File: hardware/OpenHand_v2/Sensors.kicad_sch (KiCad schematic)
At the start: 56 parts, among them U5 LM324, U6 LM324

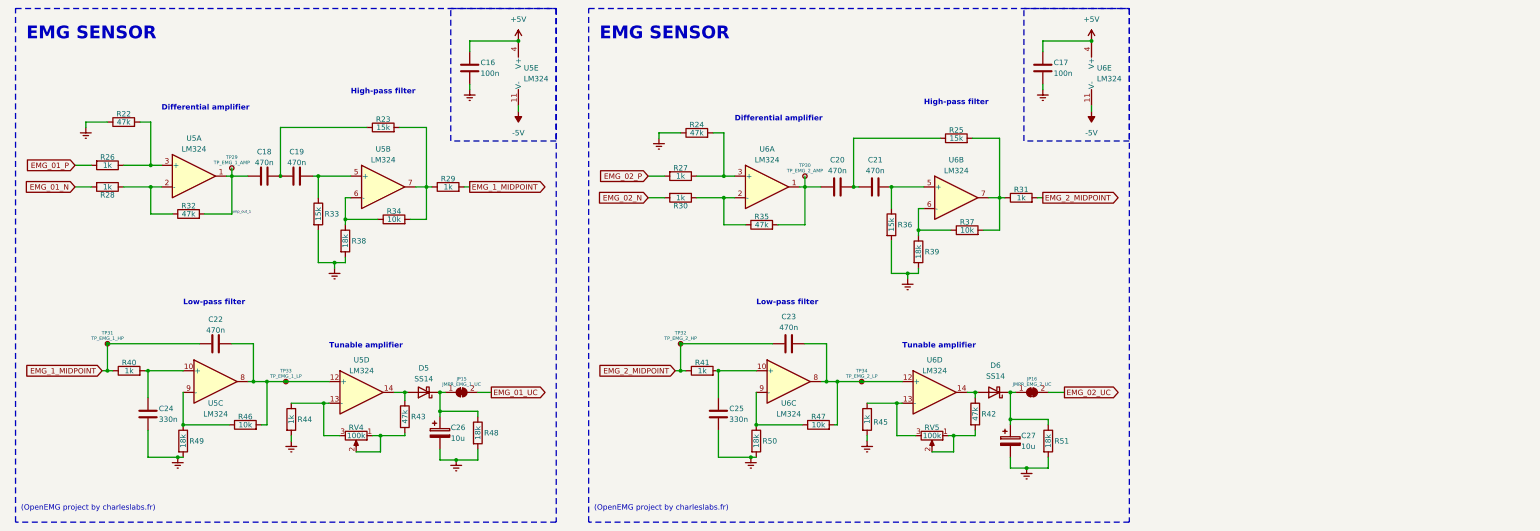
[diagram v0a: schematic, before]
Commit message: Update V2 schematic and start PCB layout
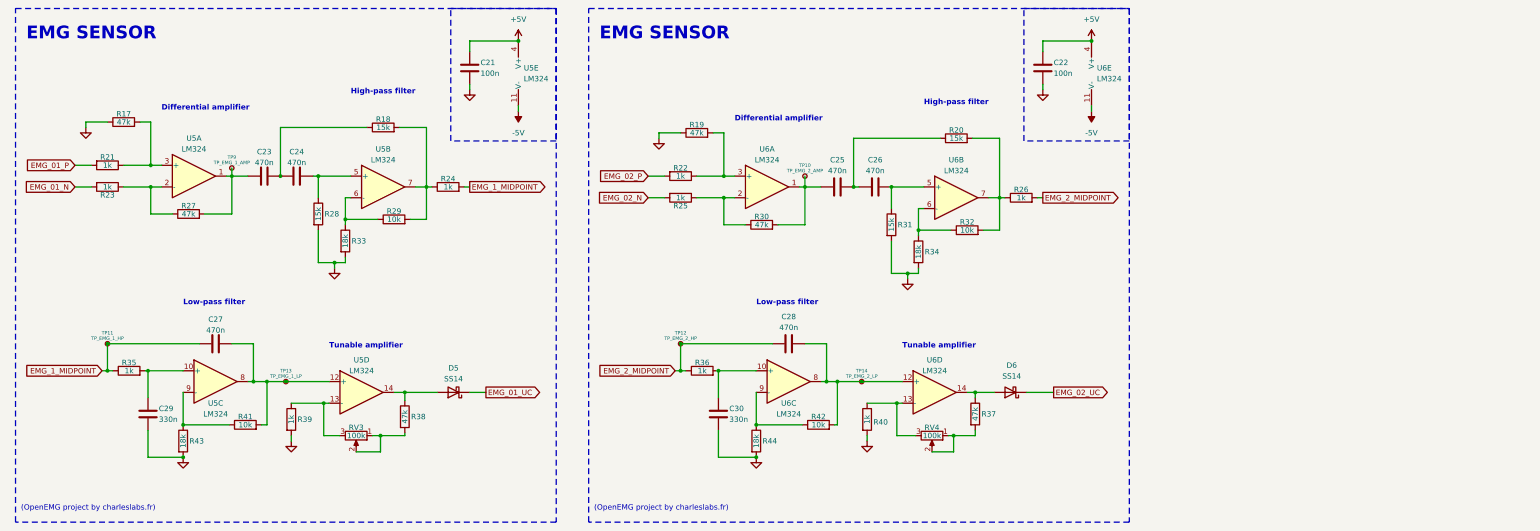
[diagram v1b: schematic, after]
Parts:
- removed C26, C27: 10u, Capacitor_SMD:C_0805_2012Metric, symbol Device:C_Polarized
- removed JP15: JMPR_EMG_1_UC, Jumper:SolderJumper-2_P1.3mm_Bridged_RoundedPad1.0x1.5mm, symbol Jumper:SolderJumper_2_Bridged
- removed JP16: JMPR_EMG_2_UC, Jumper:SolderJumper-2_P1.3mm_Bridged_RoundedPad1.0x1.5mm, symbol Jumper:SolderJumper_2_Bridged
- removed R48, R51: 18k, Resistor_SMD:R_0805_2012Metric, symbol Device:R
- renumbered C16 to C21, C17 to C22, C18 to C23, C19 to C24, C20 to C25, C21 to C26, C22 to C27, C23 to C28, C24 to C29, C25 to C30, R22 to R17, R23 to R18, R24 to R19, R25 to R20, R26 to R21, R27 to R22, R28 to R23, R29 to R24, R30 to R25, R31 to R26, R32 to R27, R33 to R28, R34 to R29, R35 to R30, R36 to R31, R37 to R32, R38 to R33, R39 to R34, R40 to R35, R41 to R36, R42 to R37, R43 to R38, R44 to R39, R45 to R40, R46 to R41, R47 to R42, R49 to R43, R50 to R44, RV4 to RV3, RV5 to RV4, TP30 to TP10, TP31 to TP11, TP32 to TP12, TP33 to TP13, TP34 to TP14, TP29 to TP9
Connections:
- net EMG_01_UC: now also D5.1 (K)
- net EMG_02_UC: now also D6.1 (K)
- net Earth renamed GND
- net amp_out_1: no longer names the net of C23.1, R27.2, TP9.1, U5.1
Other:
- moved on the sheet: D5, D6

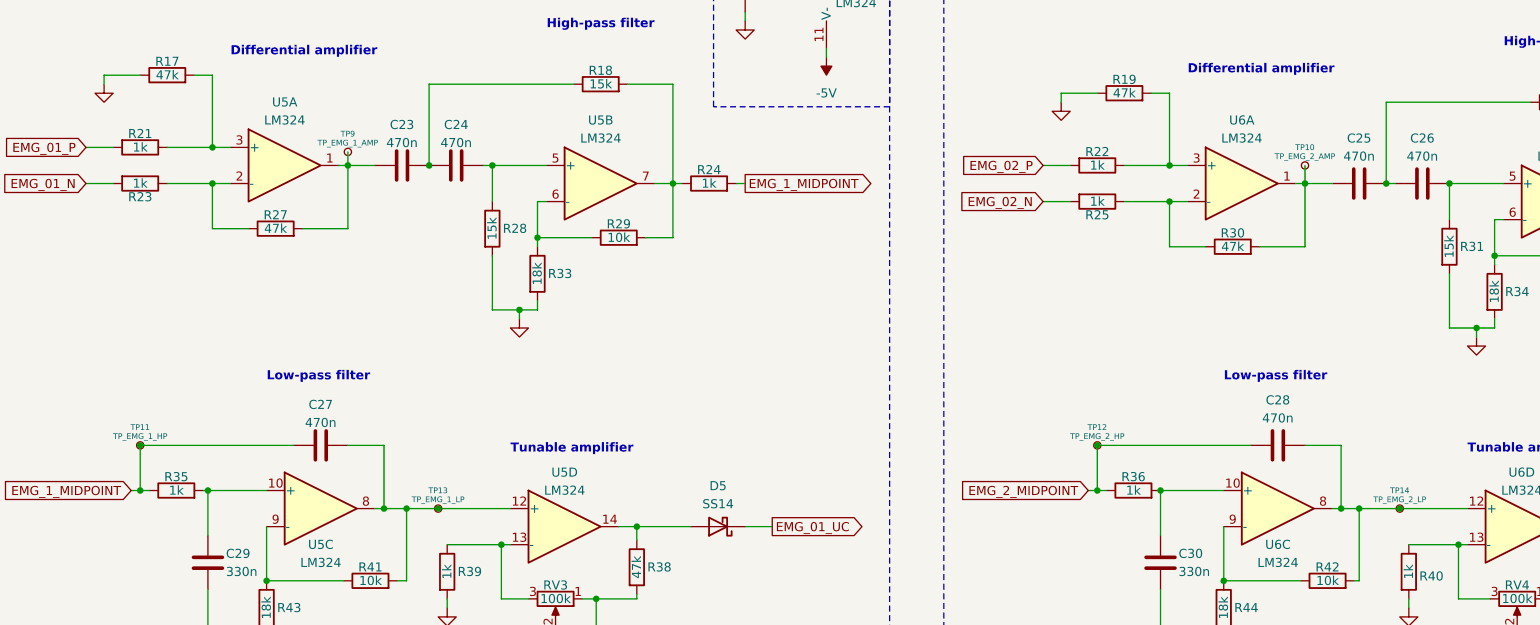
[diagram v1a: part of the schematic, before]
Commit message: Add V2 PCB and update CubeIDE config for V2
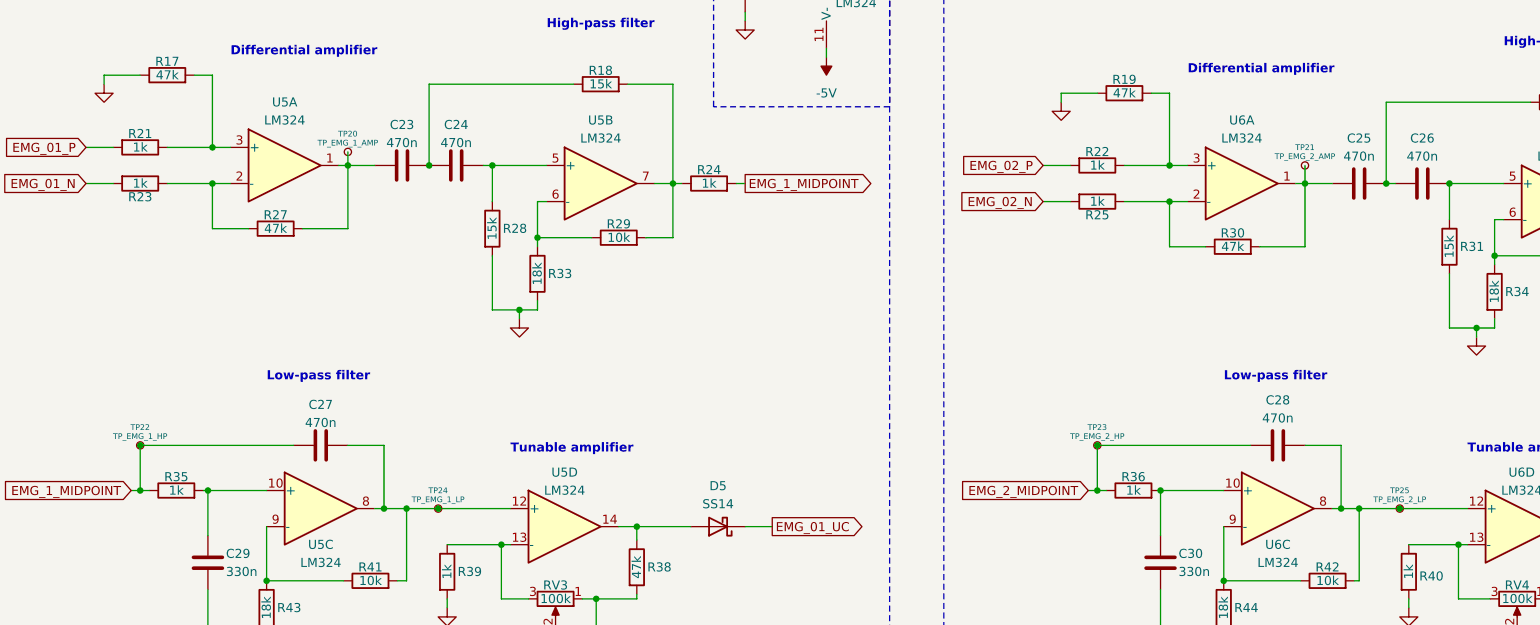
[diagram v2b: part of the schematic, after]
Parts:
- renumbered TP9 to TP20, TP10 to TP21, TP11 to TP22, TP12 to TP23, TP13 to TP24, TP14 to TP25
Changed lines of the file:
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@@
 		(dnp no)
 		(fields_autoplaced yes)
-		(property "Reference" "#PWR051"
+		(property "Reference" "#PWR053"
 			(at 270.51 29.21 0)
 			(effects
@@
 			(project "OpenHand_v2"
 				(path "/f1fbd835-8408-4592-854c-2fbec9d052ec/286dde41-8068-419e-b7de-6276970410d8"
-					(reference "#PWR051")
+					(reference "#PWR053")
 					(unit 1)
 				)
@@
 		(dnp no)
 		(fields_autoplaced yes)
-		(property "Reference" "#PWR053"
+		(property "Reference" "#PWR055"
 			(at 259.08 43.18 0)
 			(effects
@@
 			(project "OpenHand_v2"
 				(path "/f1fbd835-8408-4592-854c-2fbec9d052ec/286dde41-8068-419e-b7de-6276970410d8"
-					(reference "#PWR053")
+					(reference "#PWR055")
 					(unit 1)
 				)
@@
 		(dnp no)
 		(fields_autoplaced yes)
-		(property "Reference" "#PWR063"
+		(property "Reference" "#PWR065"
 			(at 191.77 129.54 0)
 			(effects
@@
 			(project "OpenHand_v2"
 				(path "/f1fbd835-8408-4592-854c-2fbec9d052ec/286dde41-8068-419e-b7de-6276970410d8"
-					(reference "#PWR063")
+					(reference "#PWR065")
 					(unit 1)
 				)
@@
 		(on_board yes)
 		(dnp no)
-		(property "Reference" "TP11"
+		(property "Reference" "TP22"
 			(at 39.37 93.98 0)
 			(effects
@@
 			(project "OpenHand_v2"
 				(path "/f1fbd835-8408-4592-854c-2fbec9d052ec/286dde41-8068-419e-b7de-6276970410d8"
-					(reference "TP11")
+					(reference "TP22")
 					(unit 1)
 				)
@@
 		(dnp no)
 		(fields_autoplaced yes)
-		(property "Reference" "#PWR057"
+		(property "Reference" "#PWR059"
 			(at 168.91 54.61 0)
 			(effects
@@
 			(project "OpenHand_v2"
 				(path "/f1fbd835-8408-4592-854c-2fbec9d052ec/286dde41-8068-419e-b7de-6276970410d8"
-					(reference "#PWR057")
+					(reference "#PWR059")
 					(unit 1)
 				)
@@
 		(on_board yes)
 		(dnp no)
-		(property "Reference" "TP13"
+		(property "Reference" "TP24"
 			(at 81.28 102.87 0)
 			(effects
@@
 			(project "OpenHand_v2"
 				(path "/f1fbd835-8408-4592-854c-2fbec9d052ec/286dde41-8068-419e-b7de-6276970410d8"
-					(reference "TP13")
+					(reference "TP24")
 					(unit 1)
 				)
@@
 		(dnp no)
 		(fields_autoplaced yes)
-		(property "Reference" "#PWR061"
+		(property "Reference" "#PWR063"
 			(at 217.805 125.73 0)
 			(effects
@@
 			(project "OpenHand_v2"
 				(path "/f1fbd835-8408-4592-854c-2fbec9d052ec/286dde41-8068-419e-b7de-6276970410d8"
-					(reference "#PWR061")
+					(reference "#PWR063")
 					(unit 1)
 				)
@@
 		(dnp no)
 		(fields_autoplaced yes)
-		(property "Reference" "#PWR052"
+		(property "Reference" "#PWR054"
 			(at 124.46 43.18 0)
 			(effects
@@
 			(project "OpenHand_v2"
 				(path "/f1fbd835-8408-4592-854c-2fbec9d052ec/286dde41-8068-419e-b7de-6276970410d8"
-					(reference "#PWR052")
+					(reference "#PWR054")
 					(unit 1)
 				)
@@
 		(on_board yes)
 		(dnp no)
-		(property "Reference" "TP14"
+		(property "Reference" "TP25"
 			(at 216.535 102.87 0)
 			(effects
@@
 			(project "OpenHand_v2"
 				(path "/f1fbd835-8408-4592-854c-2fbec9d052ec/286dde41-8068-419e-b7de-6276970410d8"
-					(reference "TP14")
+					(reference "TP25")
 					(unit 1)
 				)
@@
 		(dnp no)
 		(fields_autoplaced yes)
-		(property "Reference" "#PWR055"
+		(property "Reference" "#PWR057"
 			(at 270.51 44.45 0)
 			(effects
@@
 			(project "OpenHand_v2"
 				(path "/f1fbd835-8408-4592-854c-2fbec9d052ec/286dde41-8068-419e-b7de-6276970410d8"
-					(reference "#PWR055")
+					(reference "#PWR057")
 					(unit 1)
 				)
@@
 		(dnp no)
 		(fields_autoplaced yes)
-		(property "Reference" "#PWR062"
+		(property "Reference" "#PWR064"
 			(at 57.15 129.54 0)
 			(effects
@@
 			(project "OpenHand_v2"
 				(path "/f1fbd835-8408-4592-854c-2fbec9d052ec/286dde41-8068-419e-b7de-6276970410d8"
-					(reference "#PWR062")
+					(reference "#PWR064")
 					(unit 1)
 				)
@@
 		(dnp no)
 		(fields_autoplaced yes)
-		(property "Reference" "#PWR056"
+		(property "Reference" "#PWR058"
 			(at 34.29 52.07 0)
 			(effects
@@
 			(project "OpenHand_v2"
 				(path "/f1fbd835-8408-4592-854c-2fbec9d052ec/286dde41-8068-419e-b7de-6276970410d8"
-					(reference "#PWR056")
+					(reference "#PWR058")
 					(unit 1)
 				)
@@
 		(dnp no)
 		(fields_autoplaced yes)
-		(property "Reference" "#PWR059"
+		(property "Reference" "#PWR061"
 			(at 227.33 87.63 0)
 			(effects
@@
 			(project "OpenHand_v2"
 				(path "/f1fbd835-8408-4592-854c-2fbec9d052ec/286dde41-8068-419e-b7de-6276970410d8"
-					(reference "#PWR059")
+					(reference "#PWR061")
 					(unit 1)
 				)
@@
 		(dnp no)
 		(fields_autoplaced yes)
-		(property "Reference" "#PWR058"
+		(property "Reference" "#PWR060"
 			(at 92.71 85.09 0)
 			(effects
@@
 			(project "OpenHand_v2"
 				(path "/f1fbd835-8408-4592-854c-2fbec9d052ec/286dde41-8068-419e-b7de-6276970410d8"
-					(reference "#PWR058")
+					(reference "#PWR060")
 					(unit 1)
 				)
@@
 		(on_board yes)
 		(dnp no)
-		(property "Reference" "TP12"
+		(property "Reference" "TP23"
 			(at 173.99 93.98 0)
 			(effects
@@
 			(project "OpenHand_v2"
 				(path "/f1fbd835-8408-4592-854c-2fbec9d052ec/286dde41-8068-419e-b7de-6276970410d8"
-					(reference "TP12")
+					(reference "TP23")
 					(unit 1)
 				)
@@
 		(on_board yes)
 		(dnp no)
-		(property "Reference" "TP9"
+		(property "Reference" "TP20"
 			(at 68.58 52.705 0)
 			(effects
@@
 			(project "OpenHand_v2"
 				(path "/f1fbd835-8408-4592-854c-2fbec9d052ec/286dde41-8068-419e-b7de-6276970410d8"
-					(reference "TP9")
+					(reference "TP20")
 					(unit 1)
 				)
@@
 		(dnp no)
 		(fields_autoplaced yes)
-		(property "Reference" "#PWR054"
+		(property "Reference" "#PWR056"
 			(at 135.89 44.45 0)
 			(effects
@@
 			(project "OpenHand_v2"
 				(path "/f1fbd835-8408-4592-854c-2fbec9d052ec/286dde41-8068-419e-b7de-6276970410d8"
-					(reference "#PWR054")
+					(reference "#PWR056")
 					(unit 1)
 				)
@@
 		(on_board yes)
 		(dnp no)
-		(property "Reference" "TP10"
+		(property "Reference" "TP21"
 			(at 203.2 54.61 0)
 			(effects
@@
 			(project "OpenHand_v2"
 				(path "/f1fbd835-8408-4592-854c-2fbec9d052ec/286dde41-8068-419e-b7de-6276970410d8"
-					(reference "TP10")
+					(reference "TP21")
 					(unit 1)
 				)
@@
 		(dnp no)
 		(fields_autoplaced yes)
-		(property "Reference" "#PWR050"
+		(property "Reference" "#PWR052"
 			(at 135.89 29.21 0)
 			(effects
@@
 			(project "OpenHand_v2"
 				(path "/f1fbd835-8408-4592-854c-2fbec9d052ec/286dde41-8068-419e-b7de-6276970410d8"
-					(reference "#PWR050")
+					(reference "#PWR052")
 					(unit 1)
 				)
@@
 		(dnp no)
 		(fields_autoplaced yes)
-		(property "Reference" "#PWR060"
+		(property "Reference" "#PWR062"
 			(at 82.55 125.73 0)
 			(effects
@@
 			(project "OpenHand_v2"
 				(path "/f1fbd835-8408-4592-854c-2fbec9d052ec/286dde41-8068-419e-b7de-6276970410d8"
-					(reference "#PWR060")
+					(reference "#PWR062")
 					(unit 1)
 				)

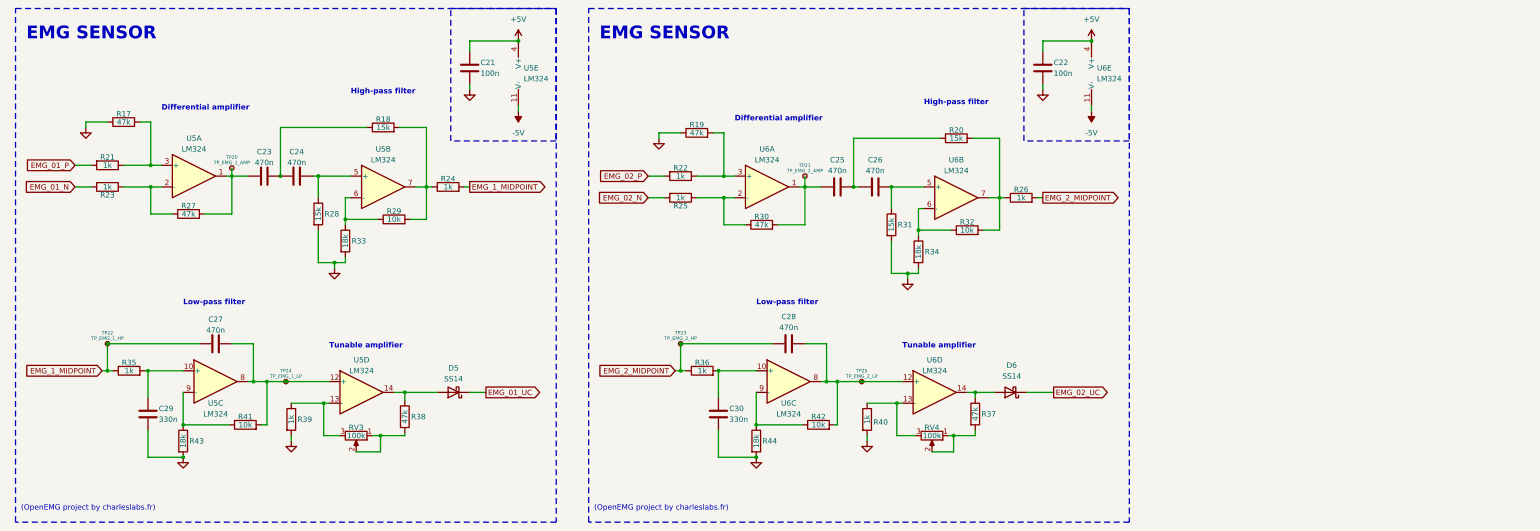
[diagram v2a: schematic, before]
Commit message: EMG sensor quickfix, upadte ADC and DMA config
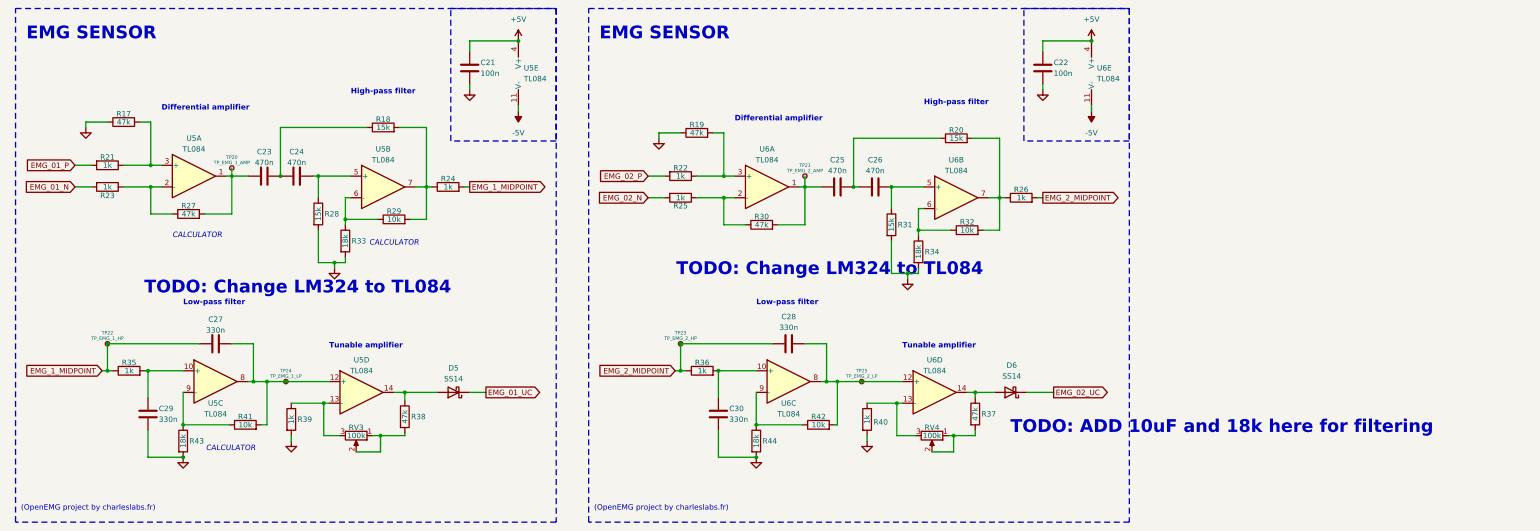
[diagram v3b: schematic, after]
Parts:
- C27, C28: value 470n -> 330n
- U5, U6: value LM324 -> TL084
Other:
- note added: "CALCULATOR"
- note added: "TODO: ADD 10uF and 18k here for filtering"
- note added: "TODO: Change LM324 to TL084"
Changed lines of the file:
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@@
 		)
 	)
+	(text "TODO: Change LM324 to TL084"
+		(exclude_from_sim no)
+		(at 48.006 85.09 0)
+		(effects
+			(font
+				(size 3 3)
+				(thickness 0.6)
+				(bold yes)
+			)
+			(justify left bottom)
+		)
+	)
 	(text "Low-pass filter"
 		(exclude_from_sim no)
@@
 		)
 	)
+	(text "CALCULATOR"
+		(exclude_from_sim no)
+		(at 106.68 72.898 0)
+		(effects
+			(font
+				(size 1.27 1.27)
+				(italic yes)
+			)
+			(href "https://www.jotrin.com/tool/details/YFGTLBQJSQ")
+		)
+	)
+	(text "CALCULATOR"
+		(exclude_from_sim no)
+		(at 60.452 71.12 0)
+		(effects
+			(font
+				(size 1.27 1.27)
+				(italic yes)
+			)
+			(href "https://onechip.com/differential-amplifier-using-op-amp-calculator.html")
+		)
+	)
 	(text "Differential amplifier"
 		(exclude_from_sim no)
@@
 		)
 	)
+	(text "TODO: ADD 10uF and 18k here for filtering"
+		(exclude_from_sim no)
+		(at 251.46 117.856 0)
+		(effects
+			(font
+				(size 3 3)
+				(thickness 0.6)
+				(bold yes)
+			)
+			(justify left bottom)
+		)
+	)
 	(text "High-pass filter"
 		(exclude_from_sim no)
@@
 		)
 	)
+	(text "TODO: Change LM324 to TL084"
+		(exclude_from_sim no)
+		(at 172.974 80.772 0)
+		(effects
+			(font
+				(size 3 3)
+				(thickness 0.6)
+				(bold yes)
+			)
+			(justify left bottom)
+		)
+	)
 	(text "(OpenEMG project by charleslabs.fr)"
 		(exclude_from_sim no)
@@
 		)
 	)
+	(text "CALCULATOR"
+		(exclude_from_sim no)
+		(at 68.326 121.158 0)
+		(effects
+			(font
+				(size 1.27 1.27)
+				(italic yes)
+			)
+			(href "https://www.jotrin.com/tool/details/YSFDQDTLBQJSQ")
+		)
+	)
 	(text "Tunable amplifier"
 		(exclude_from_sim no)
@@
 			)
 		)
-		(property "Value" "LM324"
+		(property "Value" "TL084"
 			(at 233.68 102.87 0)
 			(effects
@@
 			)
 		)
-		(property "Value" "LM324"
+		(property "Value" "TL084"
 			(at 64.77 113.03 0)
 			(effects
@@
 			)
 		)
-		(property "Value" "LM324"
+		(property "Value" "TL084"
 			(at 194.31 53.34 0)
 			(effects
@@
 			)
 		)
-		(property "Value" "LM324"
+		(property "Value" "TL084"
 			(at 104.14 53.34 0)
 			(effects
@@
 			)
 		)
-		(property "Value" "LM324"
+		(property "Value" "TL084"
 			(at 199.39 113.03 0)
 			(effects
@@
 			)
 		)
-		(property "Value" "LM324"
+		(property "Value" "TL084"
 			(at 59.69 50.8 0)
 			(effects
@@
 			)
 		)
-		(property "Value" "LM324"
+		(property "Value" "TL084"
 			(at 271.78 34.29 0)
 			(effects
@@
 			)
 		)
-		(property "Value" "470n"
+		(property "Value" "330n"
 			(at 64.77 93.345 90)
 			(effects
@@
 			)
 		)
-		(property "Value" "470n"
+		(property "Value" "330n"
 			(at 199.39 92.71 90)
 			(effects
@@
 			)
 		)
-		(property "Value" "LM324"
+		(property "Value" "TL084"
 			(at 238.76 55.88 0)
 			(effects
@@
 			)
 		)
-		(property "Value" "LM324"
+		(property "Value" "TL084"
 			(at 99.06 102.87 0)
 			(effects
@@
 		(dnp no)
 		(property "Reference" "R23"
-			(at 39.37 61.595 90)
+			(at 39.37 61.722 90)
 			(effects
 				(font
@@
 			)
 		)
-		(property "Value" "LM324"
+		(property "Value" "TL084"
 			(at 137.16 34.29 0)
 			(effects

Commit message: Update SW part, prepare for simple presentation
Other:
- note added: "TODO: ADD PASSIVE FILTERING HERE (CAP AND RES TO GND SHOULD DO)"
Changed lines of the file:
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@@
+		)
+	)
+	(text "TODO:\nADD PASSIVE FILTERING HERE\n(CAP AND RES TO GND SHOULD DO)"
+		(exclude_from_sim no)
+		(at 129.286 115.57 0)
+		(effects
+			(font
+				(size 1.27 1.27)
+			)
+			(justify top)
 		)
 	)
